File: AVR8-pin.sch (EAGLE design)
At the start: 4 parts

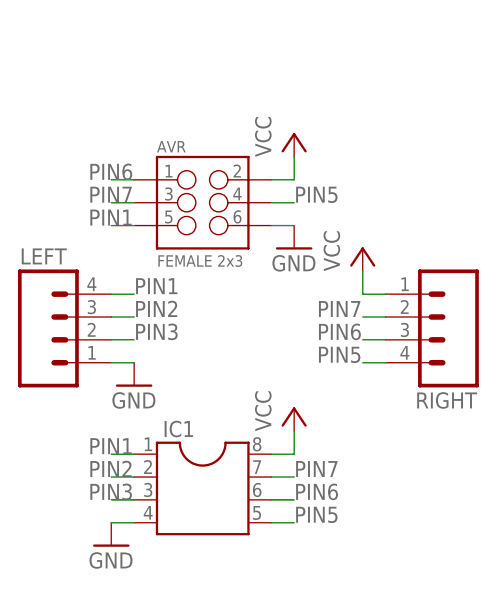
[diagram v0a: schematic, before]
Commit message: Oriented the AVR header correctly instead of the jacked up usbtinyisp cable
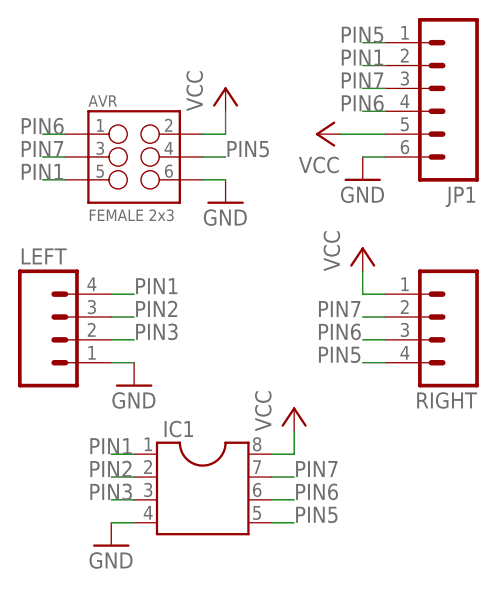
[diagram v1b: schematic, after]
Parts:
- added JP1: (no value), SparkFun-Connectors:M06SILK_FEMALE_PTH
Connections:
- net GND: now also JP1.6
- net PIN1: now also JP1.2
- net PIN5: now also JP1.1
- net PIN6: now also JP1.4
- net PIN7: now also JP1.3
- net VCC: now also JP1.5
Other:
- moved on the sheet: AVR
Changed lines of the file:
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@@
 <?xml version="1.0" encoding="utf-8"?>
 <!DOCTYPE eagle SYSTEM "eagle.dtd">
-<eagle version="7.4.0">
+<eagle version="7.5.0">
 <drawing>
 <settings>
@@
 <part name="GND3" library="supply1" deviceset="GND" device=""/>
 <part name="P+3" library="supply1" deviceset="VCC" device=""/>
+<part name="JP1" library="SparkFun-Connectors" deviceset="M06" device="SILK_FEMALE_PTH"/>
+<part name="GND4" library="supply1" deviceset="GND" device=""/>
+<part name="P+4" library="supply1" deviceset="VCC" device=""/>
 </parts>
 <sheets>
@@
 <instances>
 <instance part="IC1" gate="G$1" x="27.94" y="58.42"/>
-<instance part="AVR" gate="G$1" x="27.94" y="88.9"/>
-<instance part="P+2" gate="VCC" x="38.1" y="96.52"/>
-<instance part="GND2" gate="1" x="38.1" y="83.82"/>
+<instance part="AVR" gate="G$1" x="20.32" y="93.98"/>
+<instance part="P+2" gate="VCC" x="30.48" y="101.6"/>
+<instance part="GND2" gate="1" x="30.48" y="88.9"/>
 <instance part="GND1" gate="1" x="17.78" y="50.8"/>
 <instance part="LEFT" gate="G$1" x="12.7" y="73.66"/>
@@
 <instance part="GND3" gate="1" x="20.32" y="68.58"/>
 <instance part="P+3" gate="VCC" x="38.1" y="66.04"/>
+<instance part="JP1" gate="G$1" x="53.34" y="101.6" rot="R180"/>
+<instance part="GND4" gate="1" x="45.72" y="91.44"/>
+<instance part="P+4" gate="VCC" x="40.64" y="96.52" rot="R90"/>
 </instances>
 <busses>
@@
 <segment>
 <pinref part="AVR" gate="G$1" pin="6"/>
-<wire x1="35.56" y1="86.36" x2="38.1" y2="86.36" width="0.1524" layer="91"/>
+<wire x1="27.94" y1="91.44" x2="30.48" y2="91.44" width="0.1524" layer="91"/>
 <pinref part="GND2" gate="1" pin="GND"/>
 </segment>
@@
 <pinref part="GND3" gate="1" pin="GND"/>
 </segment>
+<segment>
+<pinref part="JP1" gate="G$1" pin="6"/>
+<wire x1="48.26" y1="93.98" x2="45.72" y2="93.98" width="0.1524" layer="91"/>
+<pinref part="GND4" gate="1" pin="GND"/>
+</segment>
 </net>
 <net name="VCC" class="0">
@@
 <pinref part="AVR" gate="G$1" pin="2"/>
 <pinref part="P+2" gate="VCC" pin="VCC"/>
-<wire x1="35.56" y1="91.44" x2="38.1" y2="91.44" width="0.1524" layer="91"/>
-<wire x1="38.1" y1="91.44" x2="38.1" y2="93.98" width="0.1524" layer="91"/>
+<wire x1="27.94" y1="96.52" x2="30.48" y2="96.52" width="0.1524" layer="91"/>
+<wire x1="30.48" y1="96.52" x2="30.48" y2="99.06" width="0.1524" layer="91"/>
 </segment>
 <segment>
@@
 <pinref part="P+3" gate="VCC" pin="VCC"/>
 </segment>
+<segment>
+<pinref part="JP1" gate="G$1" pin="5"/>
+<wire x1="48.26" y1="96.52" x2="43.18" y2="96.52" width="0.1524" layer="91"/>
+<pinref part="P+4" gate="VCC" pin="VCC"/>
+</segment>
 </net>
 <net name="PIN6" class="0">
 <segment>
 <pinref part="AVR" gate="G$1" pin="1"/>
-<wire x1="20.32" y1="91.44" x2="17.78" y2="91.44" width="0.1524" layer="91"/>
-<label x="15.24" y="91.44" size="1.778" layer="95"/>
+<wire x1="12.7" y1="96.52" x2="10.16" y2="96.52" width="0.1524" layer="91"/>
+<label x="7.62" y="96.52" size="1.778" layer="95"/>
 </segment>
 <segment>
@@
 <label x="38.1" y="55.88" size="1.778" layer="95"/>
 </segment>
+<segment>
+<pinref part="JP1" gate="G$1" pin="4"/>
+<wire x1="48.26" y1="99.06" x2="45.72" y2="99.06" width="0.1524" layer="91"/>
+<label x="43.18" y="99.06" size="1.778" layer="95"/>
+</segment>
 </net>
 <net name="PIN7" class="0">
 <segment>
 <pinref part="AVR" gate="G$1" pin="3"/>
-<wire x1="20.32" y1="88.9" x2="17.78" y2="88.9" width="0.1524" layer="91"/>
-<label x="15.24" y="88.9" size="1.778" layer="95"/>
+<wire x1="12.7" y1="93.98" x2="10.16" y2="93.98" width="0.1524" layer="91"/>
+<label x="7.62" y="93.98" size="1.778" layer="95"/>
 </segment>
 <segment>
@@
 <label x="38.1" y="58.42" size="1.778" layer="95"/>
 </segment>
+<segment>
+<pinref part="JP1" gate="G$1" pin="3"/>
+<wire x1="48.26" y1="101.6" x2="45.72" y2="101.6" width="0.1524" layer="91"/>
+<label x="43.18" y="101.6" size="1.778" layer="95"/>
+</segment>
 </net>
 <net name="PIN1" class="0">
 <segment>
 <pinref part="AVR" gate="G$1" pin="5"/>
-<wire x1="20.32" y1="86.36" x2="17.78" y2="86.36" width="0.1524" layer="91"/>
-<label x="15.24" y="86.36" size="1.778" layer="95"/>
+<wire x1="12.7" y1="91.44" x2="10.16" y2="91.44" width="0.1524" layer="91"/>
+<label x="7.62" y="91.44" size="1.778" layer="95"/>
 </segment>
 <segment>
@@
 <label x="15.24" y="60.96" size="1.778" layer="95"/>
 </segment>
+<segment>
+<pinref part="JP1" gate="G$1" pin="2"/>
+<wire x1="48.26" y1="104.14" x2="45.72" y2="104.14" width="0.1524" layer="91"/>
+<label x="43.18" y="104.14" size="1.778" layer="95"/>
+</segment>
 </net>
 <net name="PIN5" class="0">
 <segment>
 <pinref part="AVR" gate="G$1" pin="4"/>
-<wire x1="35.56" y1="88.9" x2="38.1" y2="88.9" width="0.1524" layer="91"/>
-<label x="38.1" y="88.9" size="1.778" layer="95"/>
+<wire x1="27.94" y1="93.98" x2="30.48" y2="93.98" width="0.1524" layer="91"/>
+<label x="30.48" y="93.98" size="1.778" layer="95"/>
 </segment>
 <segment>
@@
 <label x="38.1" y="53.34" size="1.778" layer="95"/>
 </segment>
-</net>
+<segment>
+<pinref part="JP1" gate="G$1" pin="1"/>
+<wire x1="48.26" y1="106.68" x2="45.72" y2="106.68" width="0.1524" layer="91"/>
+<label x="43.18" y="106.68" size="1.778" layer="95"/>
+</segment>
+</net>
